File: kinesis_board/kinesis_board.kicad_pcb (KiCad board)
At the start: 2 copper layers, 145 x 100 mm, 40 parts, among them J1 RIGHT_13_TOP, J10 LEFT_13_DOWN, J2 RIGHT_13_DOWN, J3 THUMB_RIGHT_SPC_KB600, J4 THUMB_RIGHT_SPC, J5 THUMB_LEFT_BAK, J6 THUMB_LEFT_BAK_KB600, J7 LEFT_1x24, J8 RIGHT_1x24, J9 LEFT_13_TOP

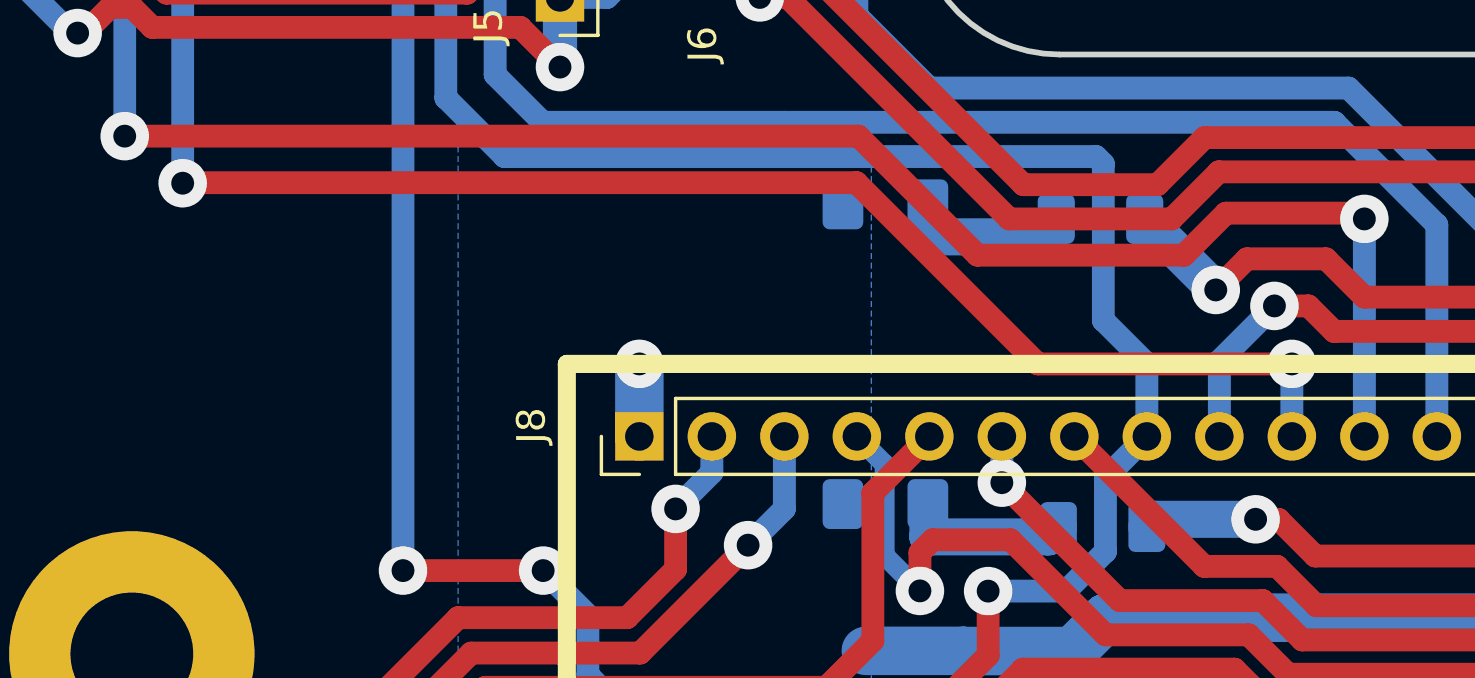
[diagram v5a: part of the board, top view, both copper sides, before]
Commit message: added forgotten vias
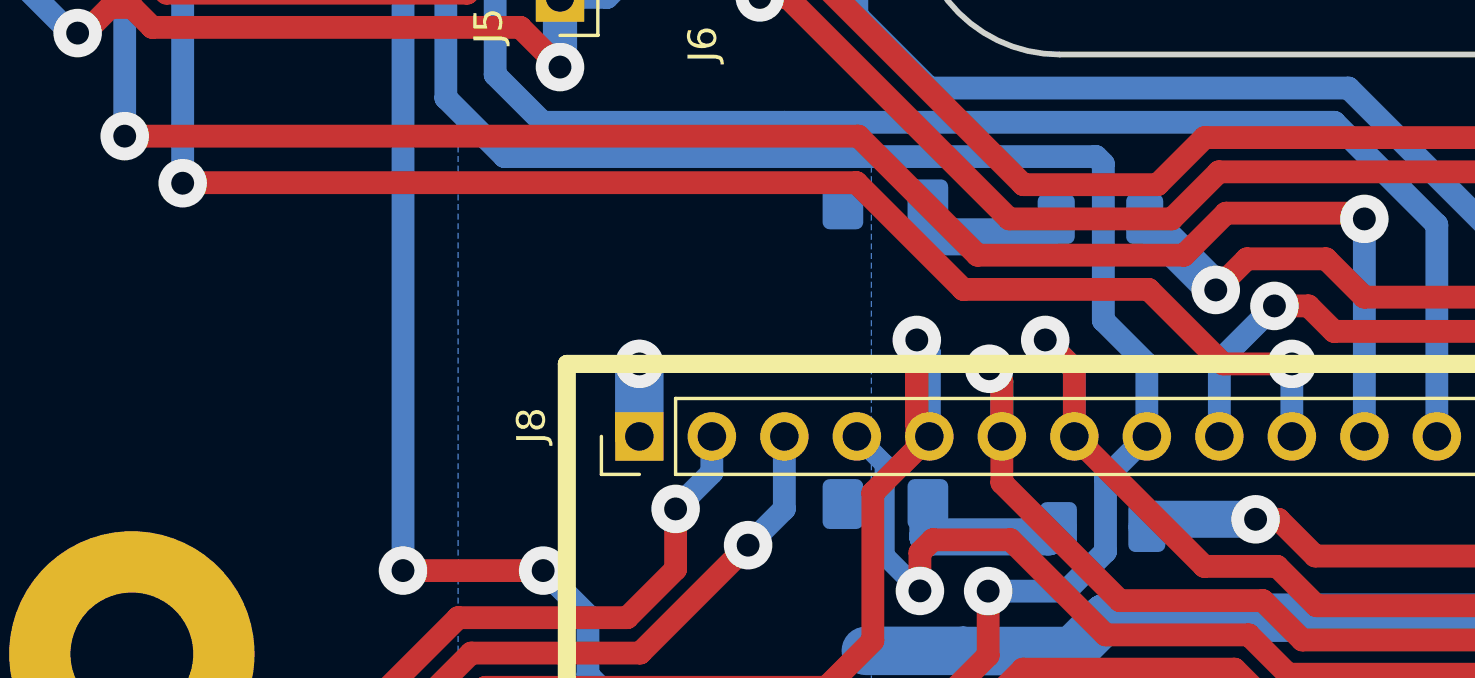
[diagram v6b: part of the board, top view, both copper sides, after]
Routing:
- net /ROW_7: track 77.3 -> 89.0 mm, vias 1 -> 2
- net /ROW_6: track 151.7 -> 159.3 mm, vias 1 -> 2
- net /ROW_8: track 172.9 -> 178.0 mm
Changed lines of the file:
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@@
   (segment (start 153.003443 118.889143) (end 153.003443 114.711588) (width 0.8) (layer "F.Cu") (net 11))
   (segment (start 153.003443 114.711588) (end 154.605888 113.109143) (width 0.8) (layer "F.Cu") (net 11))
+  (segment (start 169.122944 80.829143) (end 168.102944 79.809143) (width 0.8) (layer "F.Cu") (net 11))
   (segment (start 154.605888 113.109143) (end 158.691168 113.109143) (width 0.8) (layer "F.Cu") (net 11))
   (segment (start 180.536397 104.578643) (end 182.635897 102.479143) (width 0.8) (layer "F.Cu") (net 11))
@@
   (segment (start 215.445888 102.479143) (end 217.382944 100.542087) (width 0.8) (layer "F.Cu") (net 11))
   (segment (start 217.382944 100.542087) (end 217.382944 93.765031) (width 0.8) (layer "F.Cu") (net 11))
+  (segment (start 169.122944 83.189143) (end 169.122944 80.829143) (width 0.8) (layer "F.Cu") (net 11))
   (segment (start 212.738511 89.120598) (end 177.605567 89.120598) (width 0.8) (layer "F.Cu") (net 11))
   (segment (start 182.635897 102.479143) (end 215.445888 102.479143) (width 0.8) (layer "F.Cu") (net 11))
   (segment (start 173.67597 87.742169) (end 169.122944 83.189143) (width 0.8) (layer "F.Cu") (net 11))
+  (via (at 168.102944 79.809143) (size 1.7) (drill 0.8) (layers "F.Cu" "B.Cu") (net 11))
   (via (at 153.003443 118.889143) (size 1.7) (drill 0.8) (layers "F.Cu" "B.Cu") (net 11))
   (segment (start 158.102944 119.309143) (end 156.903553 119.309143) (width 0.8) (layer "B.Cu") (net 11))
+  (segment (start 169.122944 83.189143) (end 169.122944 80.829143) (width 0.8) (layer "B.Cu") (net 11))
   (segment (start 154.442944 119.309143) (end 153.882944 118.749143) (width 0.4) (layer "B.Cu") (net 11))
   (segment (start 151.102944 118.889143) (end 153.003443 118.889143) (width 0.8) (layer "B.Cu") (net 11))
@@
   (segment (start 156.602944 119.309143) (end 155.302333 119.309143) (width 0.4) (layer "B.Cu") (net 11))
   (segment (start 143.352944 123.809144) (end 146.182943 123.809144) (width 0.8) (layer "B.Cu") (net 11))
+  (segment (start 169.122944 80.829143) (end 168.102944 79.809143) (width 0.8) (layer "B.Cu") (net 11))
   (segment (start 153.003443 118.889143) (end 154.022944 118.889143) (width 0.8) (layer "B.Cu") (net 11))
   (segment (start 146.182943 123.809144) (end 151.102944 118.889143) (width 0.8) (layer "B.Cu") (net 11))
@@
   (segment (start 149.392944 108.519143) (end 147.052944 110.859143) (width 0.8) (layer "F.Cu") (net 12))
   (segment (start 143.153444 126.908644) (end 144.992944 125.069144) (width 0.8) (layer "F.Cu") (net 12))
+  (segment (start 166.582944 83.189143) (end 166.582944 81.258992) (width 0.8) (layer "F.Cu") (net 12))
   (segment (start 177.108511 90.320598) (end 212.241455 90.320598) (width 0.8) (layer "F.Cu") (net 12))
   (segment (start 166.582944 84.809143) (end 170.71597 88.942169) (width 0.8) (layer "F.Cu") (net 12))
+  (segment (start 166.582944 84.809143) (end 166.582944 83.189143) (width 0.8) (layer "F.Cu") (net 12))
   (segment (start 159.887056 108.519143) (end 149.392944 108.519143) (width 0.8) (layer "F.Cu") (net 12))
   (segment (start 175.730082 88.942169) (end 177.108511 90.320598) (width 0.8) (layer "F.Cu") (net 12))
   (segment (start 142.452944 126.908644) (end 143.153444 126.908644) (width 0.8) (layer "F.Cu") (net 12))
+  (segment (start 166.582944 81.258992) (end 166.142944 80.818992) (width 0.8) (layer "F.Cu") (net 12))
   (segment (start 147.052944 119.749143) (end 144.992944 121.809143) (width 0.8) (layer "F.Cu") (net 12))
   (segment (start 216.112944 100.115031) (end 214.948832 101.279143) (width 0.8) (layer "F.Cu") (net 12))
   (segment (start 212.241455 90.320598) (end 216.112944 94.192087) (width 0.8) (layer "F.Cu") (net 12))
-  (via (at 166.582944 84.809143) (size 1.7) (drill 0.8) (layers "F.Cu" "B.Cu") (net 12))
+  (via (at 166.142944 80.818992) (size 1.7) (drill 0.8) (layers "F.Cu" "B.Cu") (net 12))
   (via (at 144.992944 121.809143) (size 1.7) (drill 0.8) (layers "F.Cu" "B.Cu") (net 12))
   (via (at 142.452944 126.908644) (size 1.7) (drill 0.8) (layers "F.Cu" "B.Cu") (net 12))
@@
   (segment (start 154.105888 121.809143) (end 155.302333 121.809143) (width 0.8) (layer "B.Cu") (net 12))
   (segment (start 151.945888 123.969143) (end 154.105888 121.809143) (width 0.8) (layer "B.Cu") (net 12))
+  (segment (start 166.582944 83.189143) (end 166.582944 81.258992) (width 0.8) (layer "B.Cu") (net 12))
   (segment (start 158.102944 121.809143) (end 156.903553 121.809143) (width 0.8) (layer "B.Cu") (net 12))
+  (segment (start 166.582944 81.258992) (end 166.142944 80.818992) (width 0.8) (layer "B.Cu") (net 12))
   (segment (start 142.452944 126.908644) (end 148.163443 126.908644) (width 0.8) (layer "B.Cu") (net 12))
   (segment (start 156.602944 121.809143) (end 155.585176 121.809143) (width 0.4) (layer "B.Cu") (net 12))
-  (segment (start 166.582944 83.189143) (end 166.582944 84.809143) (width 0.8) (layer "B.Cu") (net 12))
   (segment (start 144.992944 121.809143) (end 142.102944 121.809143) (width 0.8) (layer "B.Cu") (net 12))
   (segment (start 151.102944 123.969143) (end 151.945888 123.969143) (width 0.8) (layer "B.Cu") (net 12))
   (segment (start 139.065888 101.402398) (end 148.489143 91.979143) (width 0.8) (layer "F.Cu") (net 13))
+  (segment (start 163.602944 79.809143) (end 163.602944 82.749143) (width 0.8) (layer "F.Cu") (net 13))
+  (segment (start 162.063242 85.168845) (end 163.012944 84.219143) (width 0.8) (layer "F.Cu") (net 13))
   (segment (start 160.432944 91.979143) (end 162.063242 90.348845) (width 0.8) (layer "F.Cu") (net 13))
+  (segment (start 163.602944 83.629143) (end 163.602944 79.809143) (width 0.8) (layer "F.Cu") (net 13))
   (segment (start 148.489143 91.979143) (end 160.432944 91.979143) (width 0.8) (layer "F.Cu") (net 13))
-  (segment (start 162.063242 85.168845) (end 164.042944 83.189143) (width 0.8) (layer "F.Cu") (net 13))
+  (segment (start 163.012944 84.219143) (end 164.042944 83.189143) (width 0.8) (layer "F.Cu") (net 13))
+  (segment (start 163.012944 84.219143) (end 163.602944 83.629143) (width 0.8) (layer "F.Cu") (net 13))
   (segment (start 139.065888 104.772087) (end 139.065888 101.402398) (width 0.8) (layer "F.Cu") (net 13))
   (segment (start 162.063242 90.348845) (end 162.063242 85.168845) (width 0.8) (layer "F.Cu") (net 13))
+  (segment (start 163.602944 82.749143) (end 164.042944 83.189143) (width 0.8) (layer "F.Cu") (net 13))
+  (via (at 163.602944 79.809143) (size 1.7) (drill 0.8) (layers "F.Cu" "B.Cu") (net 13))
   (via (at 139.065888 104.772087) (size 1.7) (drill 0.8) (layers "F.Cu" "B.Cu") (net 13))
   (segment (start 151.972944 120.559143) (end 156.102943 120.559143) (width 0.8) (layer "B.Cu") (net 13))
   (segment (start 139.065888 104.772087) (end 139.065888 110.272087) (width 0.8) (layer "B.Cu") (net 13))
+  (segment (start 164.042944 83.189143) (end 164.042944 80.249143) (width 0.8) (layer "B.Cu") (net 13))
   (segment (start 147.272943 125.259144) (end 151.102944 121.429143) (width 0.8) (layer "B.Cu") (net 13))
   (segment (start 142.302944 125.259144) (end 147.272943 125.259144) (width 0.8) (layer "B.Cu") (net 13))
@@
   (segment (start 140.852944 123.809144) (end 140.852944 122.609753) (width 0.8) (layer "B.Cu") (net 13))
   (segment (start 151.102944 121.429143) (end 151.972944 120.559143) (width 0.8) (layer "B.Cu") (net 13))
+  (segment (start 164.042944 80.249143) (end 163.602944 79.809143) (width 0.8) (layer "B.Cu") (net 13))
   (segment (start 142.491168 116.170919) (end 140.852944 117.809143) (width 0.8) (layer "B.Cu") (net 13))
   (segment (start 140.852944 117.809143) (end 140.852944 121.008533) (width 0.8) (layer "B.Cu") (net 13))
@@
   (segment (start 174.202944 80.547143) (end 176.132944 78.617143) (width 0.8) (layer "B.Cu") (net 49))
   (segment (start 174.202944 83.189143) (end 174.202944 80.547143) (width 0.8) (layer "B.Cu") (net 49))
-  (segment (start 137.902446 74.299143) (end 161.491776 74.299143) (width 0.8) (layer "F.Cu") (net 50))
-  (segment (start 137.883389 74.3182) (end 137.902446 74.299143) (width 0.8) (layer "F.Cu") (net 50))
-  (segment (start 161.491776 74.299143) (end 167.841776 80.649143) (width 0.8) (layer "F.Cu") (net 50))
-  (segment (start 167.841776 80.649143) (end 176.742944 80.649143) (width 0.8) (layer "F.Cu") (net 50))
+  (segment (start 174.335556 80.649143) (end 171.725556 78.039143) (width 0.8) (layer "F.Cu") (net 50))
+  (segment (start 171.725556 78.039143) (end 165.231776 78.039143) (width 0.8) (layer "F.Cu") (net 50))
+  (segment (start 176.742944 80.649143) (end 174.335556 80.649143) (width 0.8) (layer "F.Cu") (net 50))
+  (segment (start 165.231776 78.039143) (end 161.491776 74.299143) (width 0.8) (layer "F.Cu") (net 50))
+  (segment (start 161.491776 74.299143) (end 137.902446 74.299143) (width 0.8) (layer "F.Cu") (net 50))
+  (segment (start 137.902446 74.299143) (end 137.883389 74.3182) (width 0.8) (layer "F.Cu") (net 50))
   (via (at 137.883389 74.3182) (size 1.7) (drill 0.8) (layers "F.Cu" "B.Cu") (net 50))
   (via (at 176.742944 80.649143) (size 1.7) (drill 0.8) (layers "F.Cu" "B.Cu") (net 50))

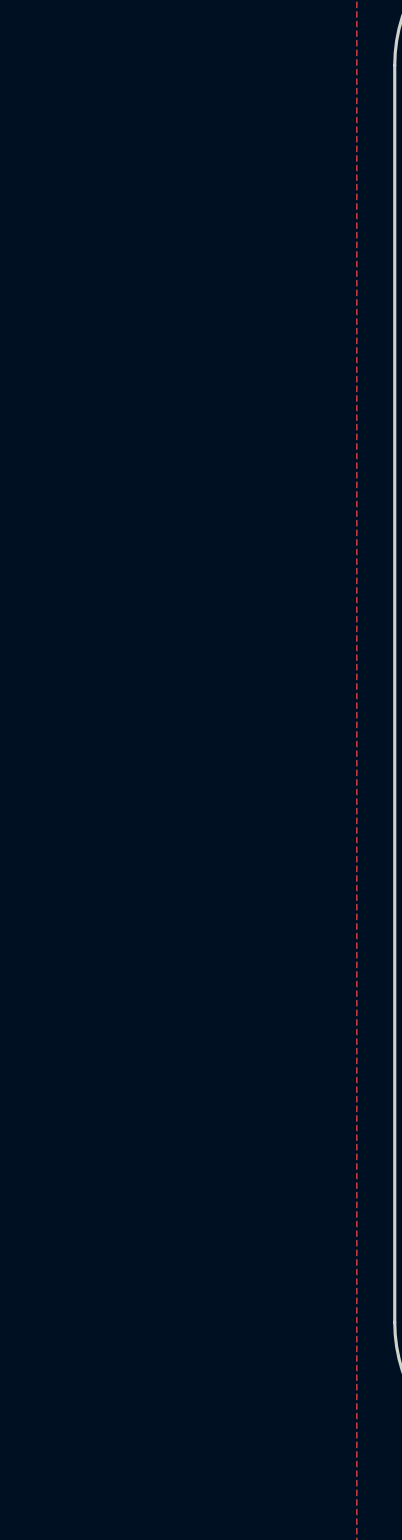
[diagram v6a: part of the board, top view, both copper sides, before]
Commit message: added fpc connector to be able to connect new fkeys keypads - not routed yet
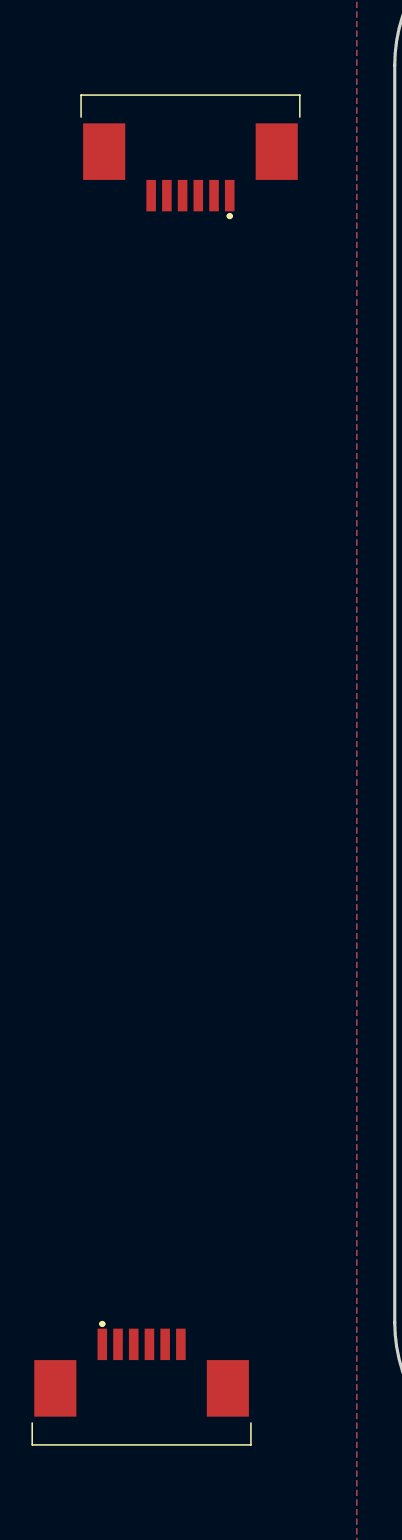
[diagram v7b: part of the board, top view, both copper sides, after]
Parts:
- added J11: RIGHT_8_TOP, dodo_conn:84953-6, F.Cu at (67.1, 56.6)
- added J12: LEFT_8_TOP, dodo_conn:84953-6, F.Cu at (64.0, 134.7)
